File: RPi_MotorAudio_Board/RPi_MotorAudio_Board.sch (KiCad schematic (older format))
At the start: 39 parts, among them J1 Audio-Jack-4, J2 SPEAKER, J3 STEP_1, J4 STEP_2, P1 Conn_02x20_Odd_Even, U1 PAM8303AAD, U2 DRV8834-VQFN

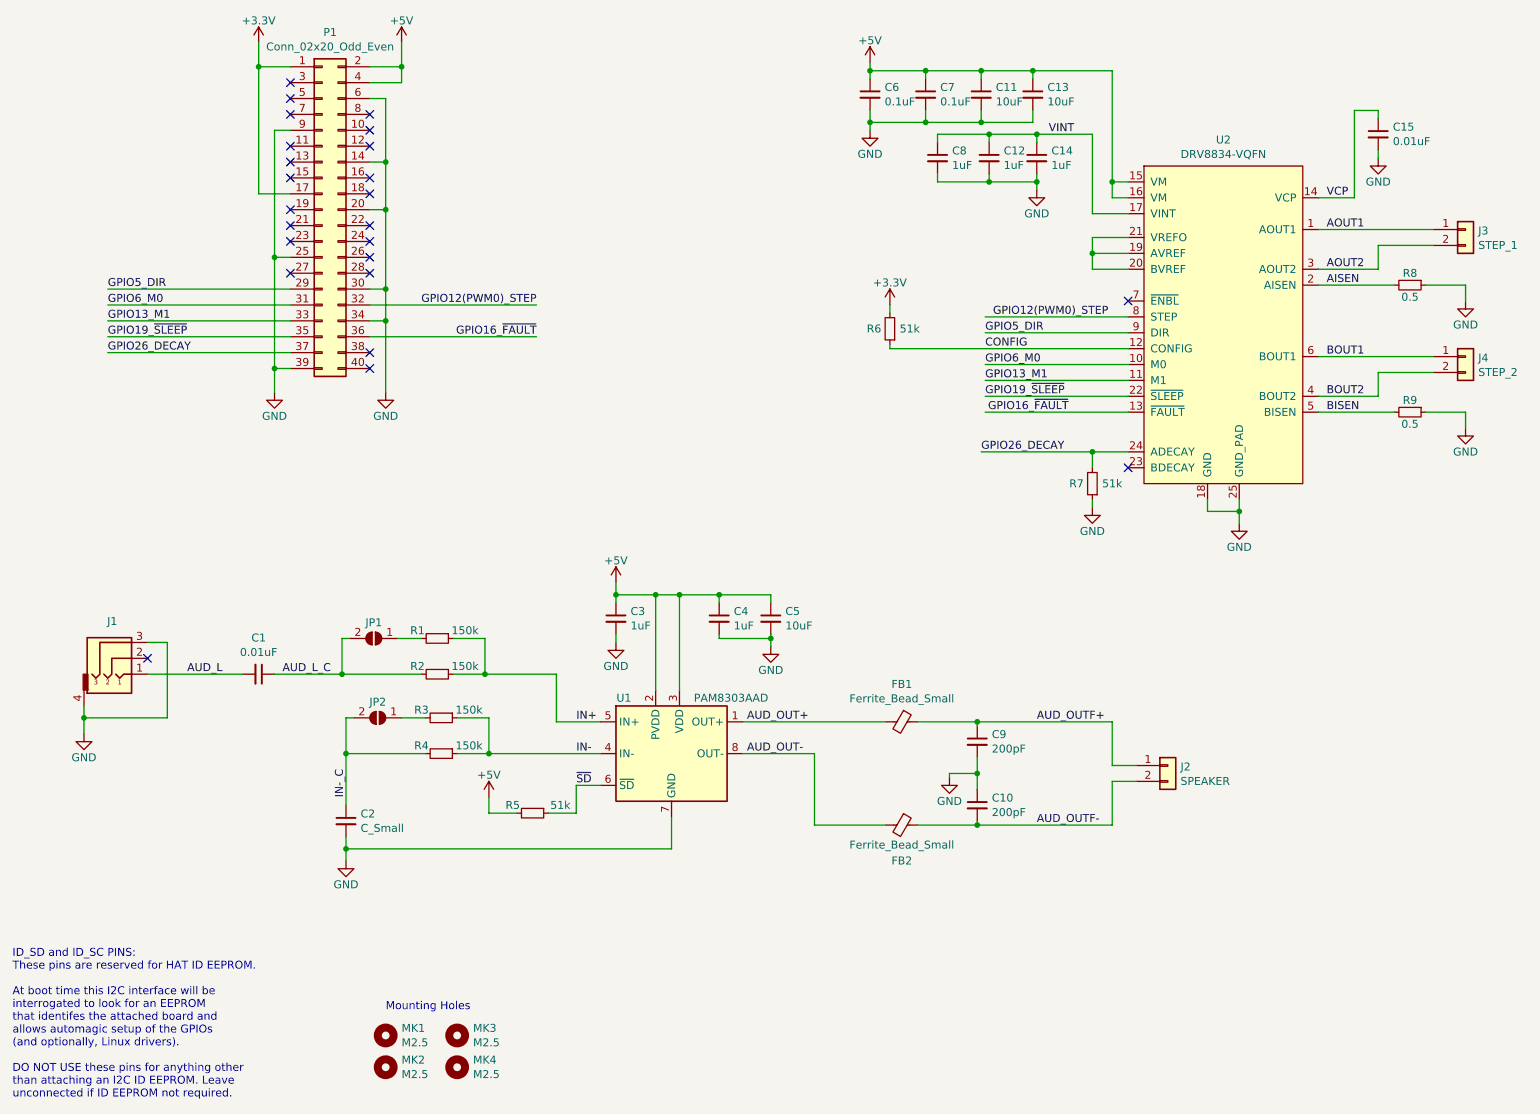
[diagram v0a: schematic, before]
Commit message: finished component associatoin
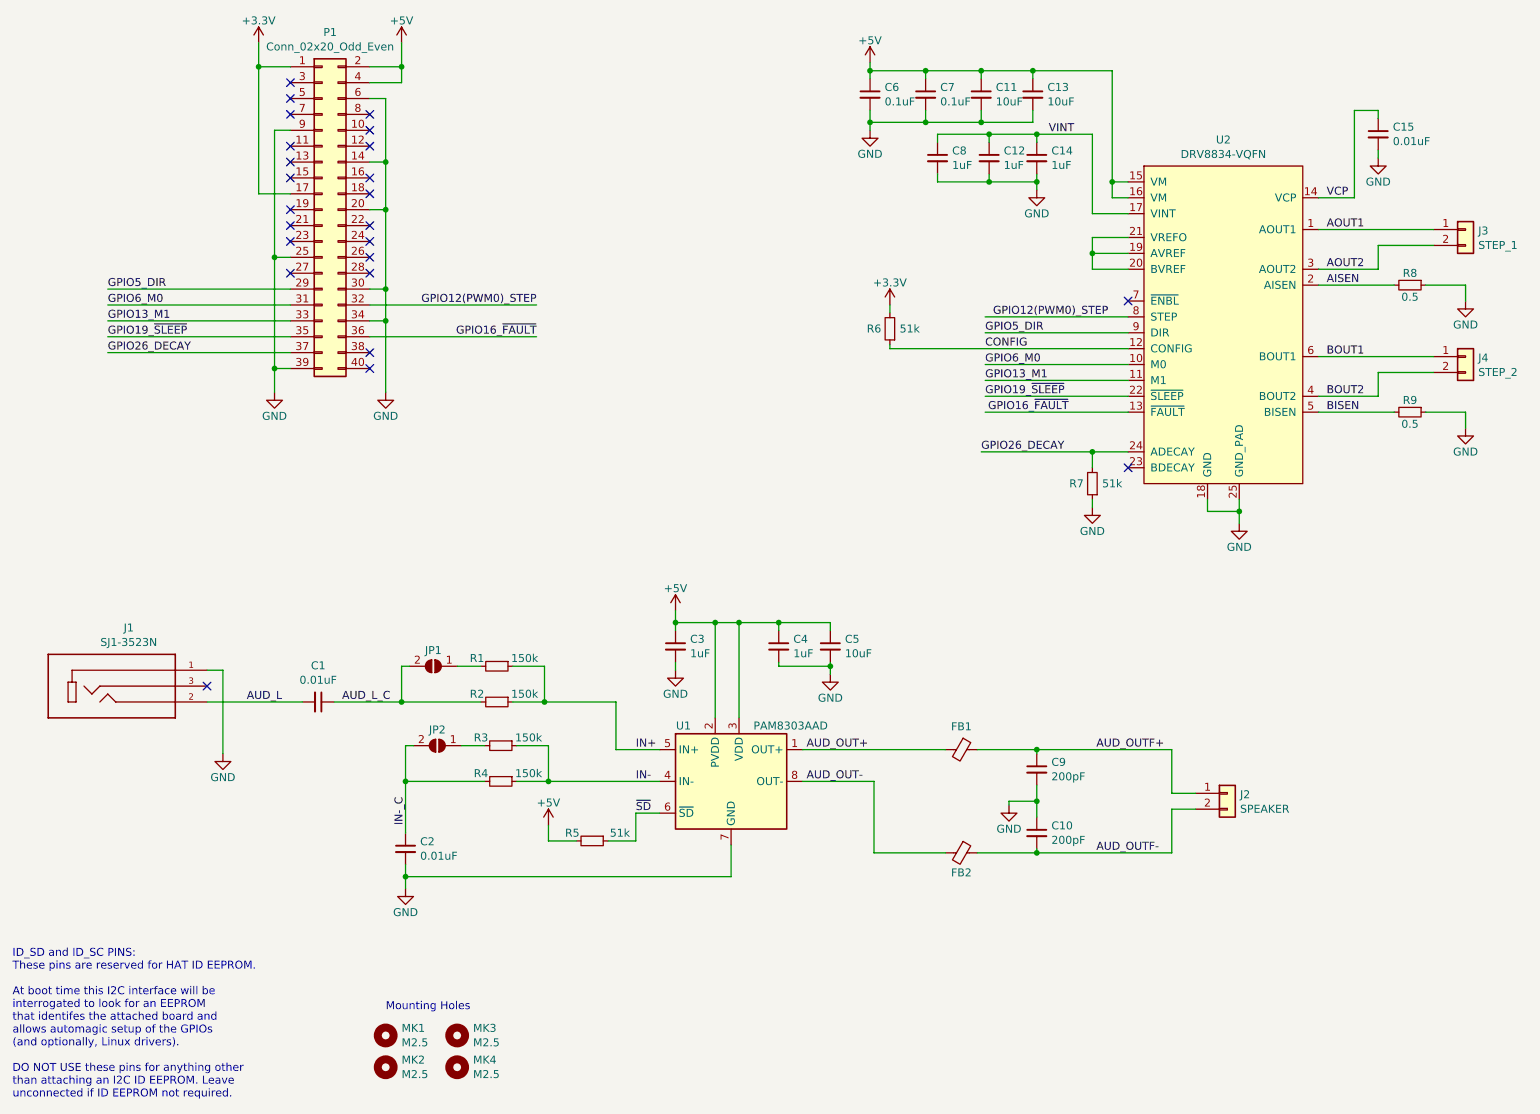
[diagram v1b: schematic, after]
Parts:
- removed J1: Audio-Jack-4, symbol Connector_DigiKey:Audio-Jack-4
- added J1: SJ1-3523N, KiCad_Offline:CUI_SJ1-3523N, symbol SJ1-3523N:SJ1-3523N
- C1, C15: footprint (none) -> Capacitors_SMD:C_0603; JLCPCB (none) -> C57112
- C10, C9: footprint (none) -> Capacitors_SMD:C_0603; JLCPCB (none) -> C1600
- C11, C13, C5: footprint (none) -> Capacitors_SMD:C_0805; JLCPCB (none) -> C15850
- C12, C14, C3, C4, C8: footprint (none) -> Capacitors_SMD:C_0603; JLCPCB (none) -> C15849
- C2: value C_Small -> 0.01uF; footprint (none) -> Capacitors_SMD:C_0603; JLCPCB (none) -> C57112
- C6, C7: footprint (none) -> Capacitors_SMD:C_0603; JLCPCB (none) -> C14663
- FB1, FB2: footprint (none) -> Capacitors_SMD:C_0603; JLCPCB (none) -> C85832
- J2, J3, J4: footprint (none) -> Connectors_Terminal_Blocks:TerminalBlock_bornier-2_P5.08mm
- JP1, JP2: footprint (none) -> UserFootprints:Inductor_SMD_3.0mm_x_3.0mm
- MK1, MK2, MK3, MK4: footprint MountingHole:MountingHole_2.7mm_M2.5 -> Mounting_Holes:MountingHole_2.7mm_M2.5
- R1, R2, R3, R4: footprint (none) -> Capacitors_SMD:C_0603; JLCPCB (none) -> C22807
- R5, R6, R7: footprint (none) -> Capacitors_SMD:C_0603; JLCPCB (none) -> C23196
- R8, R9: footprint (none) -> Resistors_SMD:R_2512; JLCPCB (none) -> C27777
- U1: footprint (none) -> Housings_SSOP:MSOP-8_3x3mm_Pitch0.65mm; JLCPCB (none) -> C56211
- U2: footprint (none) -> KiCad_Offline:QFN50P400X400X100-25N; JLCPCB (none) -> C87672
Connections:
- net AUD_L: now also J1.2
- net GND: now also J1.1
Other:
- moved on the sheet: C1, C10, C2, C3, C4, C5, C9, FB1, FB2, J2, JP1, JP2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

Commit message: final commit before fab
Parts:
- removed MK3: M2.5, Mounting_Holes:MountingHole_2.7mm_M2.5, symbol RPi_MotorAudio_Board-rescue:Mounting_Hole-Mechanical
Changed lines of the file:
@@
-$EndComp
-$Comp
-L RPi_MotorAudio_Board-rescue:Mounting_Hole-Mechanical MK3
-U 1 1 5834FBEF
-P 3450 7200
-F 0 "MK3" H 3550 7246 50  0000 L CNN
-F 1 "M2.5" H 3550 7155 50  0000 L CNN
-F 2 "Mounting_Holes:MountingHole_2.7mm_M2.5" H 3450 7200 60  0001 C CNN
-F 3 "" H 3450 7200 60  0001 C CNN
-	1    3450 7200
-	1    0    0    -1
 $EndComp
 $Comp
